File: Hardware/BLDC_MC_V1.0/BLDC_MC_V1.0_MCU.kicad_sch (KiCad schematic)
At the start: 13 parts, among them U1 STM32G431RBTx, Y1 Crystal_GND24, Y2 Crystal

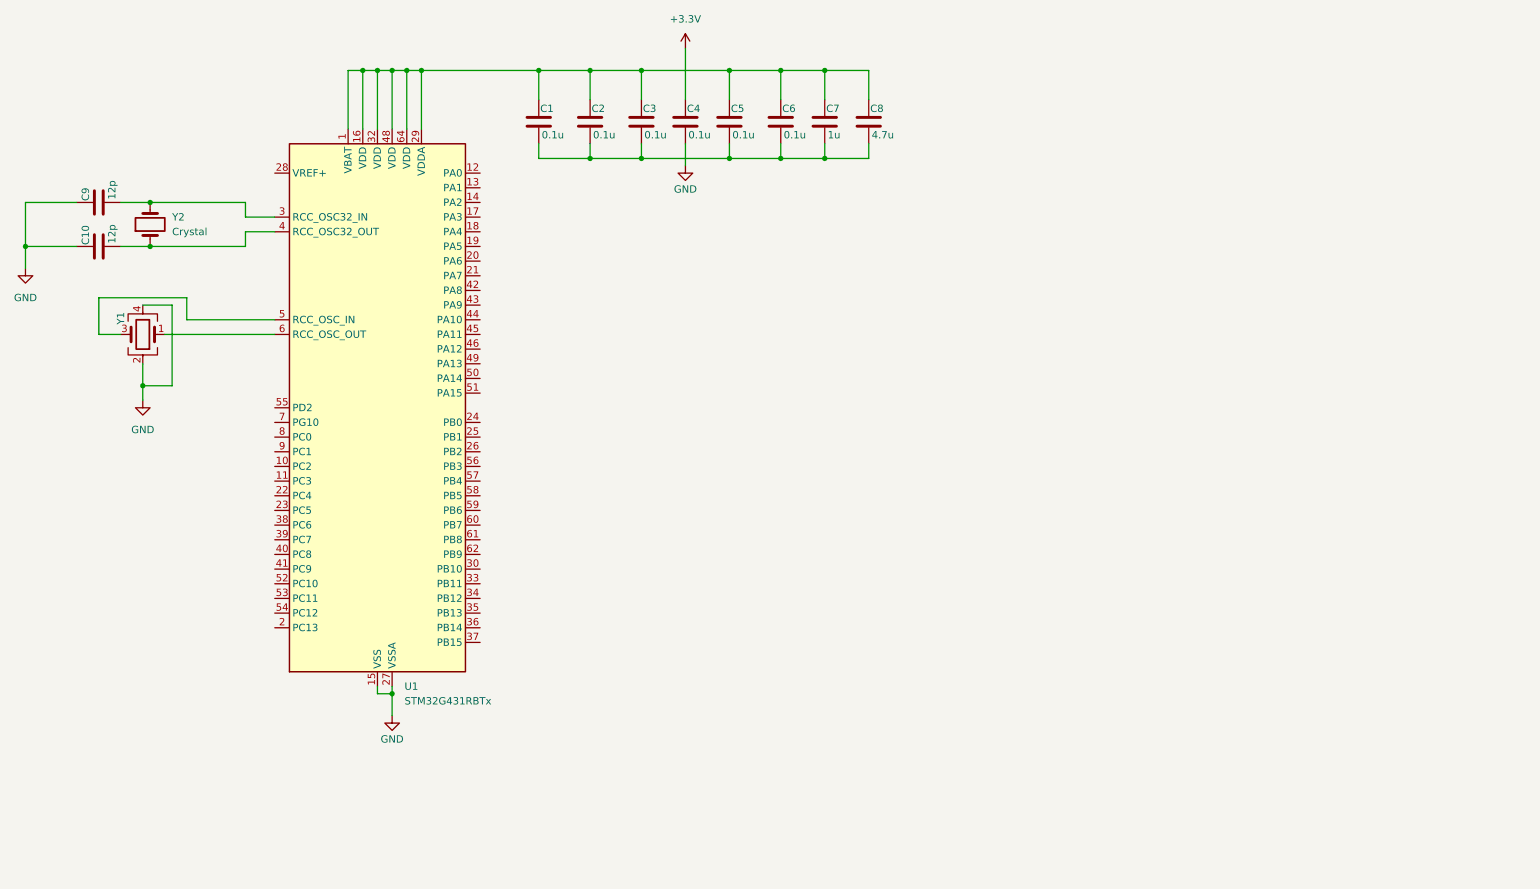
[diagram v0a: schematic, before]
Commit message: add the new edits to Buck converter sheet and edit other sheets name
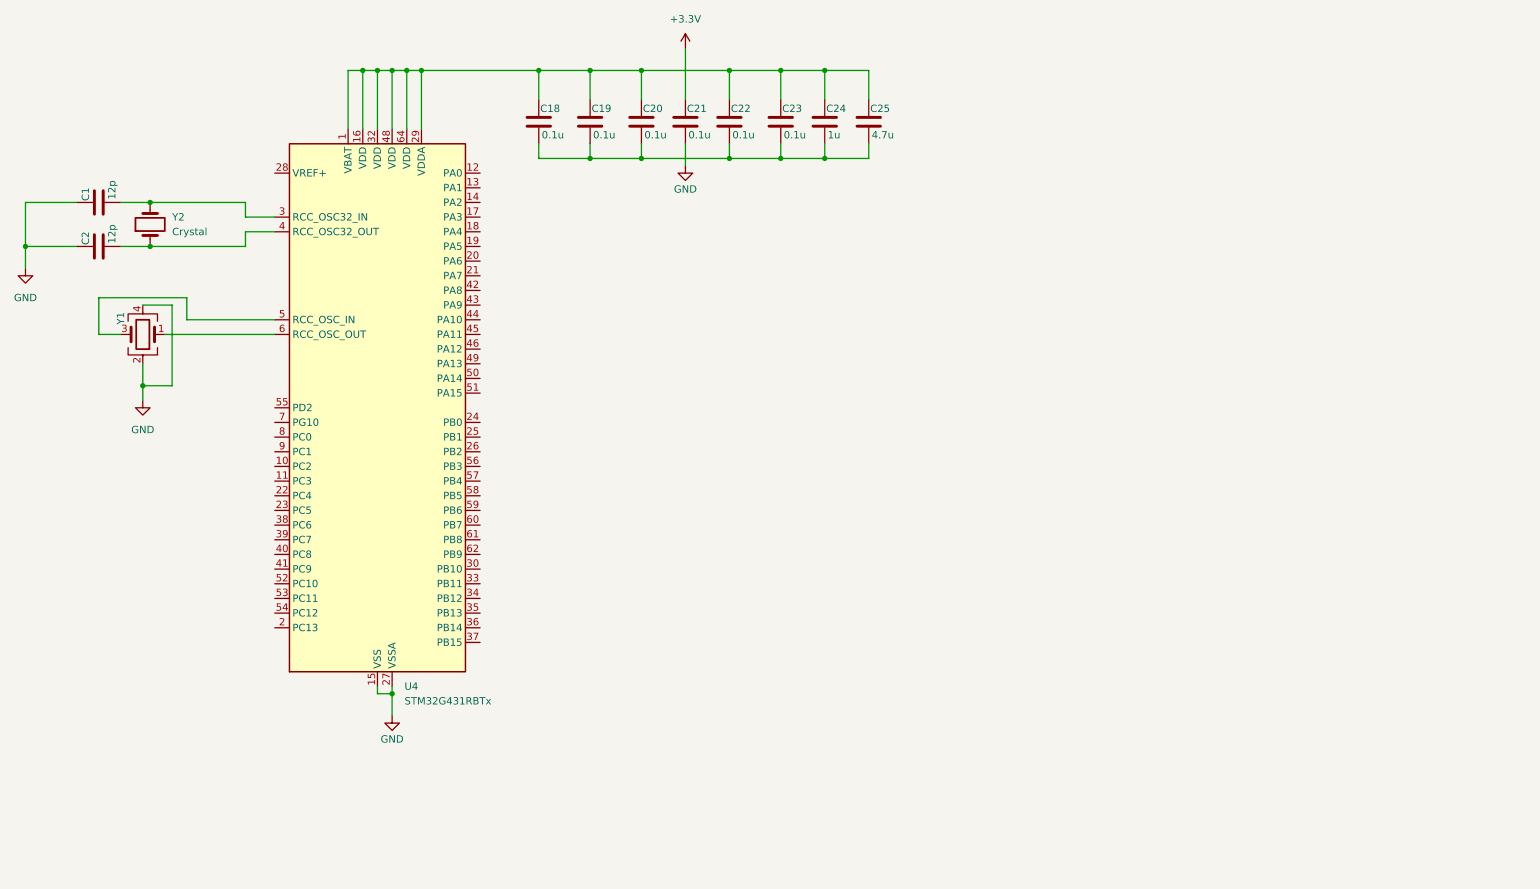
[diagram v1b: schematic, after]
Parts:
- renumbered C9 to C1, C1 to C18, C2 to C19, C10 to C2, C3 to C20, C4 to C21, C5 to C22, C6 to C23, C7 to C24, C8 to C25, U1 to U4
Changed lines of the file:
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@@
 		(on_board yes)
 		(dnp no)
-		(property "Reference" "C?"
+		(property "Reference" "C25"
 			(at 171.704 32.004 0)
 			(effects
@@
 			(project "BLDC_Motor_Driver"
 				(path "/e34fda66-7244-4ac9-bbf7-3725f03e688f/a8b67aa6-c16e-4704-8284-64b4e81a0aca"
-					(reference "C?")
+					(reference "C25")
 					(unit 1)
 				)
@@
 		(dnp no)
 		(fields_autoplaced yes)
-		(property "Reference" "U?"
+		(property "Reference" "U4"
 			(at 91.0433 132.08 0)
 			(effects
@@
 			(project "BLDC_Motor_Driver"
 				(path "/e34fda66-7244-4ac9-bbf7-3725f03e688f/a8b67aa6-c16e-4704-8284-64b4e81a0aca"
-					(reference "U?")
+					(reference "U4")
 					(unit 1)
 				)
@@
 		(on_board yes)
 		(dnp no)
-		(property "Reference" "C?"
+		(property "Reference" "C22"
 			(at 147.574 32.004 0)
 			(effects
@@
 			(project "BLDC_Motor_Driver"
 				(path "/e34fda66-7244-4ac9-bbf7-3725f03e688f/a8b67aa6-c16e-4704-8284-64b4e81a0aca"
-					(reference "C?")
+					(reference "C22")
 					(unit 1)
 				)
@@
 		(on_board yes)
 		(dnp no)
-		(property "Reference" "C?"
+		(property "Reference" "C23"
 			(at 156.464 32.004 0)
 			(effects
@@
 			(project "BLDC_Motor_Driver"
 				(path "/e34fda66-7244-4ac9-bbf7-3725f03e688f/a8b67aa6-c16e-4704-8284-64b4e81a0aca"
-					(reference "C?")
+					(reference "C23")
 					(unit 1)
 				)
@@
 		(on_board yes)
 		(dnp no)
-		(property "Reference" "C?"
+		(property "Reference" "C19"
 			(at 123.444 32.004 0)
 			(effects
@@
 			(project "BLDC_Motor_Driver"
 				(path "/e34fda66-7244-4ac9-bbf7-3725f03e688f/a8b67aa6-c16e-4704-8284-64b4e81a0aca"
-					(reference "C?")
+					(reference "C19")
 					(unit 1)
 				)
@@
 		(on_board yes)
 		(dnp no)
-		(property "Reference" "C?"
+		(property "Reference" "C21"
 			(at 139.954 32.004 0)
 			(effects
@@
 			(project "BLDC_Motor_Driver"
 				(path "/e34fda66-7244-4ac9-bbf7-3725f03e688f/a8b67aa6-c16e-4704-8284-64b4e81a0aca"
-					(reference "C?")
+					(reference "C21")
 					(unit 1)
 				)
@@
 		(on_board yes)
 		(dnp no)
-		(property "Reference" "C?"
+		(property "Reference" "C20"
 			(at 132.334 32.004 0)
 			(effects
@@
 			(project "BLDC_Motor_Driver"
 				(path "/e34fda66-7244-4ac9-bbf7-3725f03e688f/a8b67aa6-c16e-4704-8284-64b4e81a0aca"
-					(reference "C?")
+					(reference "C20")
 					(unit 1)
 				)
@@
 		(on_board yes)
 		(dnp no)
-		(property "Reference" "C?"
+		(property "Reference" "C1"
 			(at 35.814 48.006 0)
 			(effects
@@
 			(project "BLDC_Motor_Driver"
 				(path "/e34fda66-7244-4ac9-bbf7-3725f03e688f/a8b67aa6-c16e-4704-8284-64b4e81a0aca"
-					(reference "C?")
+					(reference "C1")
 					(unit 1)
 				)
@@
 		(on_board yes)
 		(dnp no)
-		(property "Reference" "Y?"
+		(property "Reference" "Y1"
 			(at 41.91 68.326 90)
 			(effects
@@
 			(project "BLDC_Motor_Driver"
 				(path "/e34fda66-7244-4ac9-bbf7-3725f03e688f/a8b67aa6-c16e-4704-8284-64b4e81a0aca"
-					(reference "Y?")
+					(reference "Y1")
 					(unit 1)
 				)
@@
 		(dnp no)
 		(fields_autoplaced yes)
-		(property "Reference" "Y?"
+		(property "Reference" "Y2"
 			(at 50.8 50.7999 90)
 			(effects
@@
 			(project "BLDC_Motor_Driver"
 				(path "/e34fda66-7244-4ac9-bbf7-3725f03e688f/a8b67aa6-c16e-4704-8284-64b4e81a0aca"
-					(reference "Y?")
+					(reference "Y2")
 					(unit 1)
 				)
@@
 		(on_board yes)
 		(dnp no)
-		(property "Reference" "C?"
+		(property "Reference" "C2"
 			(at 35.814 55.626 0)
 			(effects
@@
 			(project "BLDC_Motor_Driver"
 				(path "/e34fda66-7244-4ac9-bbf7-3725f03e688f/a8b67aa6-c16e-4704-8284-64b4e81a0aca"
-					(reference "C?")
+					(reference "C2")
 					(unit 1)
 				)
@@
 		(on_board yes)
 		(dnp no)
-		(property "Reference" "C?"
+		(property "Reference" "C18"
 			(at 114.554 32.004 0)
 			(effects
@@
 			(project "BLDC_Motor_Driver"
 				(path "/e34fda66-7244-4ac9-bbf7-3725f03e688f/a8b67aa6-c16e-4704-8284-64b4e81a0aca"
-					(reference "C?")
+					(reference "C18")
 					(unit 1)
 				)
@@
 		(on_board yes)
 		(dnp no)
-		(property "Reference" "C?"
+		(property "Reference" "C24"
 			(at 164.084 32.004 0)
 			(effects
@@
 			(project "BLDC_Motor_Driver"
 				(path "/e34fda66-7244-4ac9-bbf7-3725f03e688f/a8b67aa6-c16e-4704-8284-64b4e81a0aca"
-					(reference "C?")
-					(unit 1)
-				)
+					(reference "C24")
+					(unit 1)
+				)

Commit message: Edit Controller sheet and add oscillators for the controller
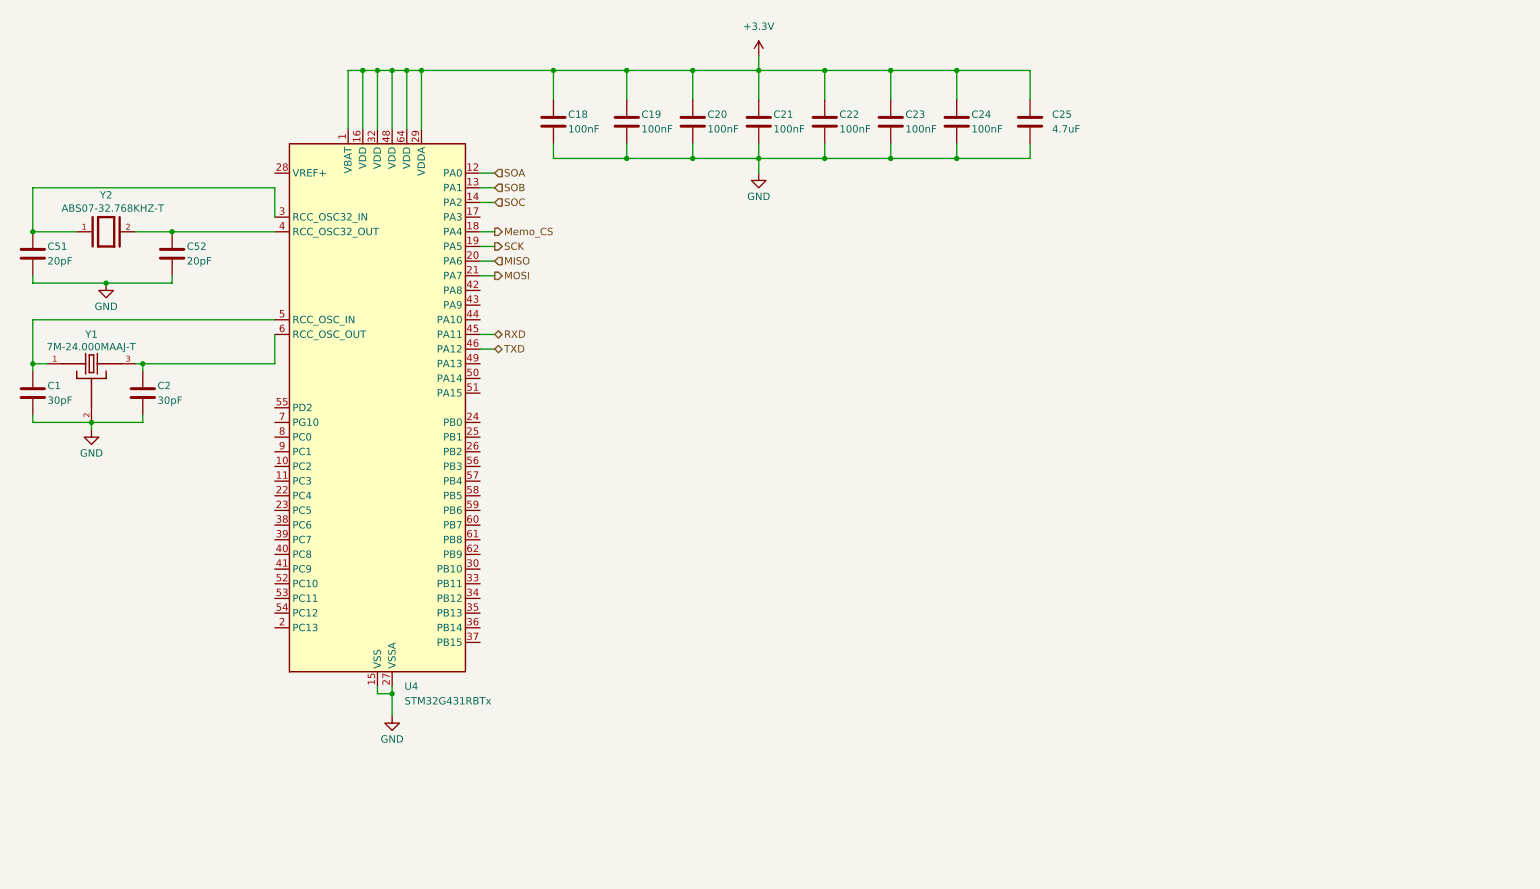
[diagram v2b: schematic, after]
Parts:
- removed Y1: Crystal_GND24, symbol Device:Crystal_GND24
- removed Y2: Crystal, symbol Device:Crystal
- added C51, C52: 20pF, Capacitor_SMD:C_0603_1608Metric, symbol Device:C
- added Y1: 7M-24.000MAAJ-T, BLDC_Motor_Driver_Components_Footprint:XTAL_7M-24.000MAAJ-T, symbol 7M-24.000MAAJ-T:7M-24.000MAAJ-T
- added Y2: ABS07-32.768KHZ-T, BLDC_Motor_Driver_Components_Footprint:XTAL_ABS07-32.768KHZ-T, symbol ABS07-32.768KHZ-T:ABS07-32.768KHZ-T
- C1, C2: value 12p -> 30pF; footprint Capacitor_SMD:C_0805_2012Metric_Pad1.18x1.45mm_HandSolder -> Capacitor_SMD:C_0603_1608Metric; Assembled (none) -> Yes; LCSC_PN (none) -> C113797; MP (none) -> CC0603JRNPO9BN300; Manufacturer YAGEO -> (none); Package 0805 -> (none)
- C18, C19, C20, C21, C22, C23: value 0.1u -> 100nF; footprint Capacitor_SMD:C_0805_2012Metric_Pad1.18x1.45mm_HandSolder -> Capacitor_SMD:C_0805_2012Metric; Assembled (none) -> Yes; LCSC Part # C49678 -> (none); LCSC_PN (none) -> C28233; MP (none) -> CL21B104KCFNNNE; Manufacturer YAGEO -> (none); Mfr. Part # CC0805KRX7R9BB104 -> (none); Package 0805 -> (none)
- C24: value 1u -> 100nF; footprint Capacitor_SMD:C_0805_2012Metric_Pad1.18x1.45mm_HandSolder -> Capacitor_SMD:C_0805_2012Metric; Assembled (none) -> Yes; LCSC_PN (none) -> C28233; MP (none) -> CL21B104KCFNNNE; Manufacturer YAGEO -> (none); Package 0805 -> (none)
- C25: value 4.7u -> 4.7uF; footprint Capacitor_SMD:C_0805_2012Metric_Pad1.18x1.45mm_HandSolder -> Capacitor_SMD:C_1206_3216Metric; Assembled (none) -> Yes; LCSC_PN (none) -> C51205; MP (none) -> CL31B475KBHNNNE; Manufacturer YAGEO -> (none); Package 0805 -> (none)
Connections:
- net +3.3V: now also C18.1, C19.1, C20.1, C22.1, C23.1, C24.1, C25.1, U4.1 (VBAT), U4.16 (VDD), U4.29 (VDDA), U4.32 (VDD), U4.48 (VDD), U4.64 (VDD)
- net GND: now also C1.2, C18.2, C19.2, C2.2, C20.2, C22.2, C23.2, C24.2, C25.2, C51.2, C52.2, Y1.2, Y1.4; no longer C1.1, C2.1
- net SOA: now reaches U4.12 (PA0)
- net SOB: now reaches U4.13 (PA1)
- net SOC: now reaches U4.14 (PA2)
- net Memo_CS: now reaches U4.18 (PA4)
- net SCK: now reaches U4.19 (PA5)
- net MISO: now reaches U4.20 (PA6)
- net MOSI: now reaches U4.21 (PA7)
- net at U4.3 (PC14): now also C51.1, Y2.1; no longer C1.2
- net at U4.4 (PC15): now also C52.1, Y2.2; no longer C2.2
- net RXD: now reaches U4.45 (PA11)
- net TXD: now reaches U4.46 (PA12)
- net at U4.5 (PF0): now also C1.1, Y1.1
- net at U4.6 (PF1): now also C2.1, Y1.3

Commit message: Edit main sheet (root)
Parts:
- added R33: 0R, Resistor_SMD:R_0603_1608Metric, symbol Device:R
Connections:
- net at C2.1, Y1.3: now also R33.1; no longer U4.6 (PF1)
- new net: R33.2, U4.6 (PF1)
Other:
- moved on the sheet: C1, C18, C19, C2, C20, C21, C22, C23, C24, C25, C51, C52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

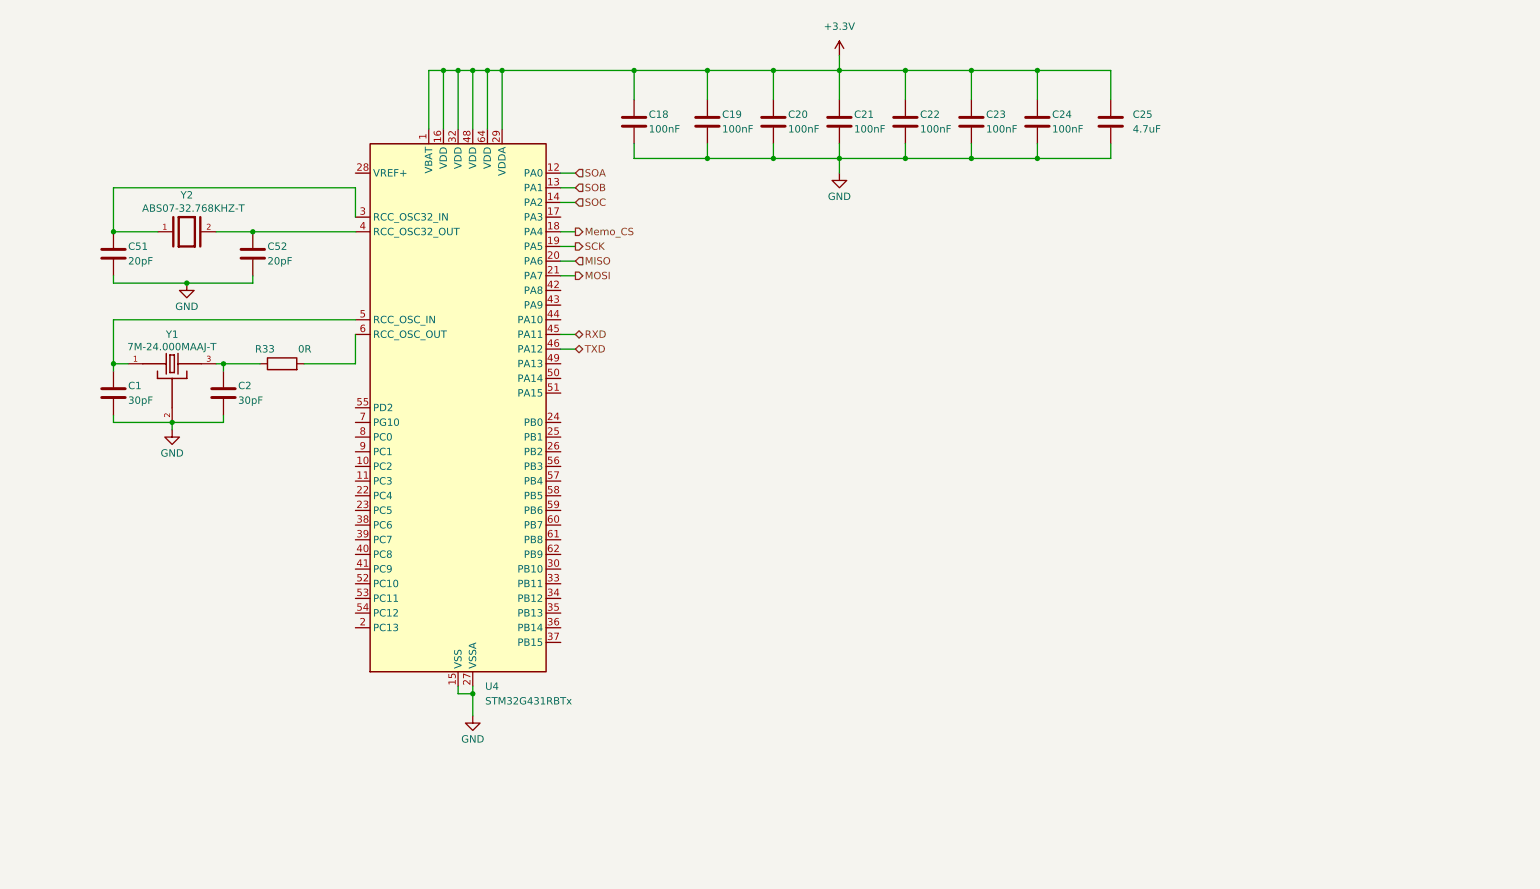
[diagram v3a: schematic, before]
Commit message: Add the USB-C connector - define the PWM pins and other enable and fault pins for gate driver
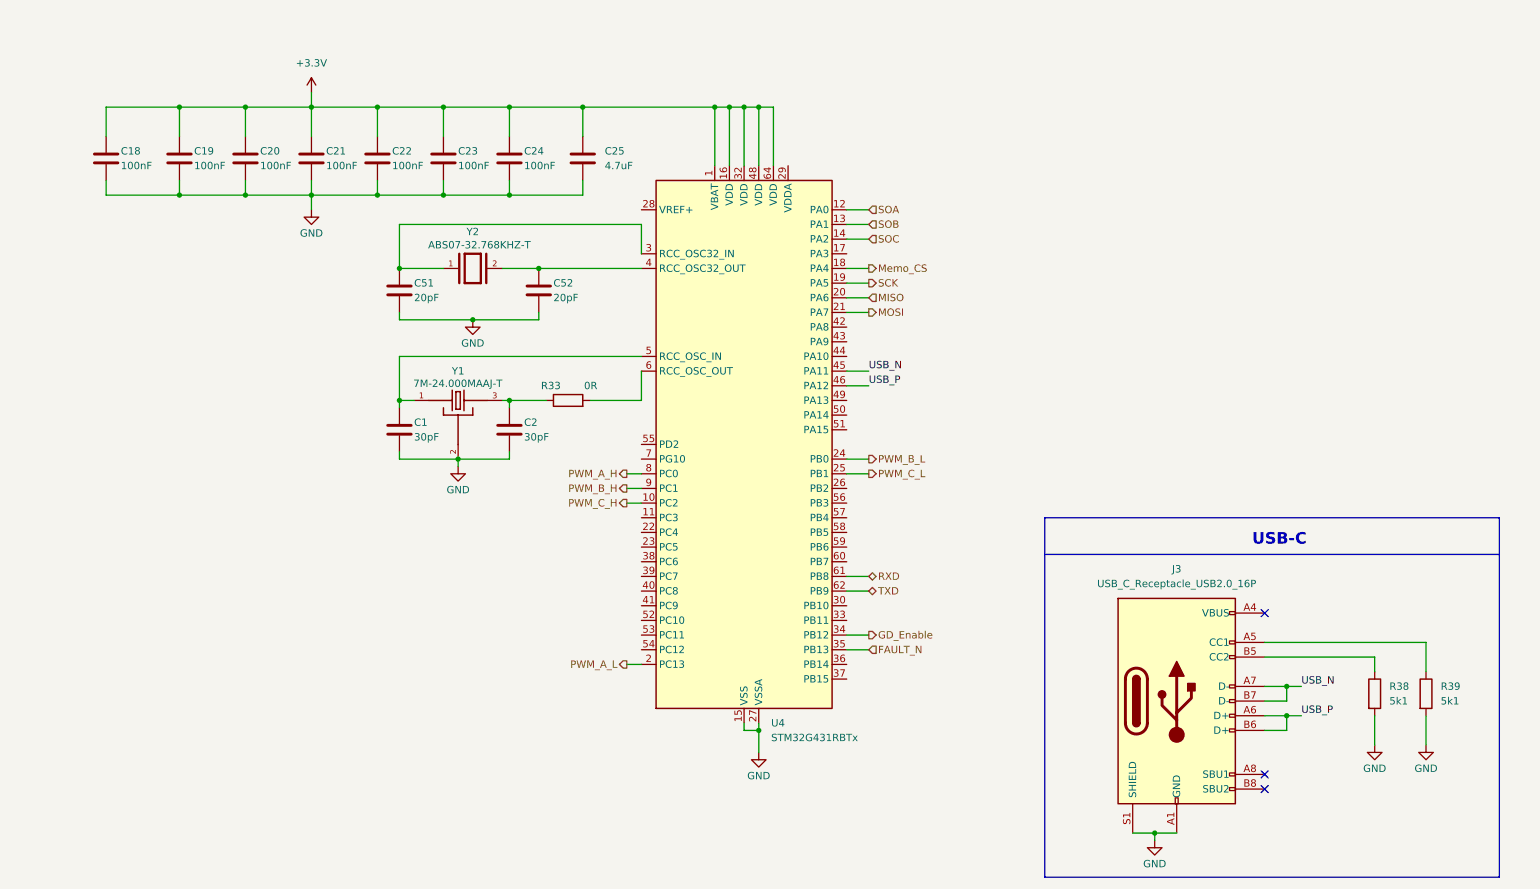
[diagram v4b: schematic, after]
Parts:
- added J3: USB_C_Receptacle_USB2.0_16P, Connector_USB:USB_C_Receptacle_GCT_USB4105-xx-A_16P_TopMnt_Horizontal, symbol Connector:USB_C_Receptacle_USB2.0_16P
- added R38, R39: 5k1, Resistor_SMD:R_0603_1608Metric, symbol Device:R
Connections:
- net +3.3V: no longer U4.29 (VDDA)
- net GND: now also J3.A1 (GND), J3.A12 (GND), J3.B1 (GND), J3.B12 (GND), J3.S1 (SHIELD), R38.2, R39.2
- net RXD: now also U4.61 (PB8); no longer U4.45 (PA11)
- net TXD: now also U4.62 (PB9); no longer U4.46 (PA12)
- net PWM_C_H: now reaches U4.10 (PC2)
- net PWM_A_L: now reaches U4.2 (PC13)
- net PWM_B_L: now reaches U4.24 (PB0)
- net PWM_C_L: now reaches U4.25 (PB1)
- net GD_Enable: now reaches U4.34 (PB12)
- net FAULT_N: now reaches U4.35 (PB13)
- net PWM_A_H: now reaches U4.8 (PC0)
- net PWM_B_H: now reaches U4.9 (PC1)
- new net: J3.B5 (CC2), R38.1
- new net: J3.A5 (CC1), R39.1
- new net: J3.A4 (VBUS), J3.A9 (VBUS), J3.B4 (VBUS), J3.B9 (VBUS)
- new net USB_N: J3.A7 (D-), J3.B7 (D-), U4.45 (PA11)
- new net USB_P: J3.A6 (D+), J3.B6 (D+), U4.46 (PA12)
- no-connect marks 0 -> 3
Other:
- note added: "USB-C"
- moved on the sheet: C1, C18, C19, C2, C20, C21, C22, C23, C24, C25, C51, C52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
